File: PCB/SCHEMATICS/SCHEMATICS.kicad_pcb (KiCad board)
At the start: 2 copper layers, 95 parts, among them IC1 CP2102-GMR, Q1 PMOS, U1 C7433, U2 AMS1117-3.3, U3 LTR-303ALS-01, U4 AMS1117-3.3, U5 LTR-303ALS-01, U6 C6482, U7 C6482

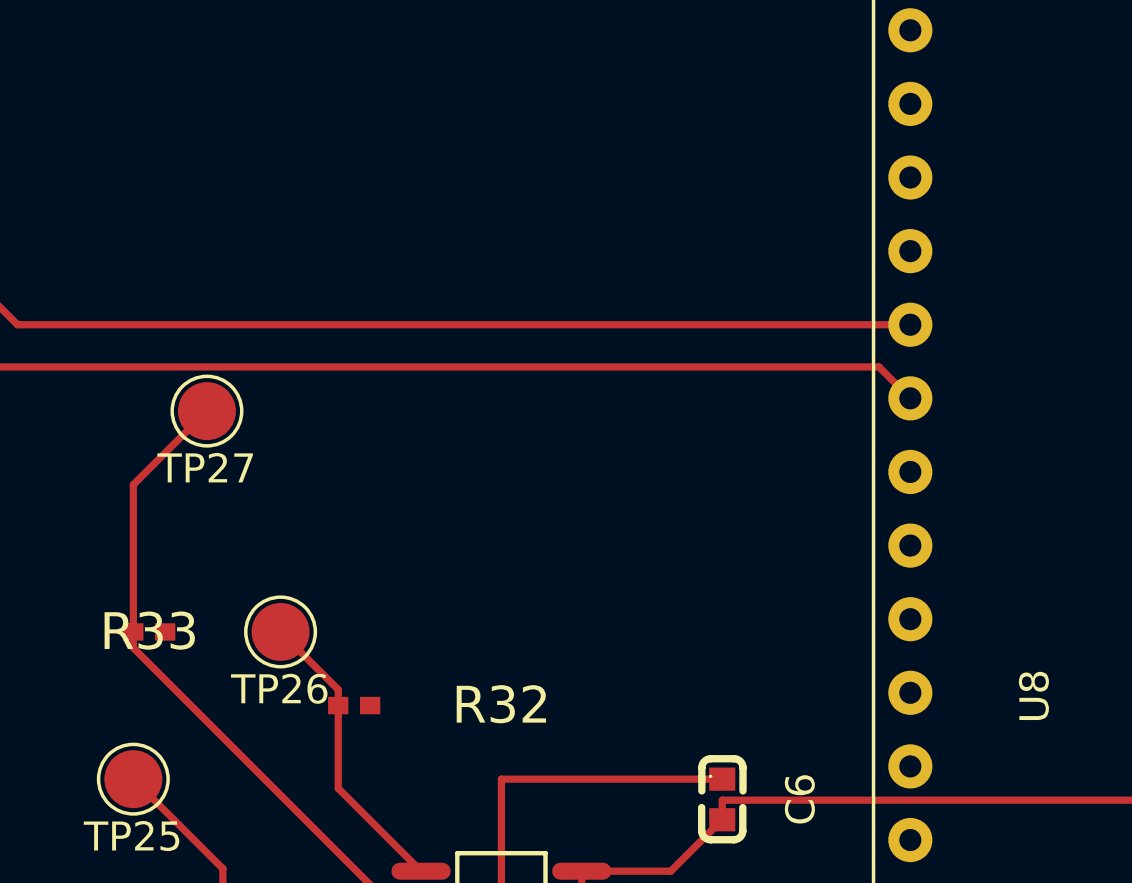
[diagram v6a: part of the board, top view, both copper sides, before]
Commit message: Creating ratsnest
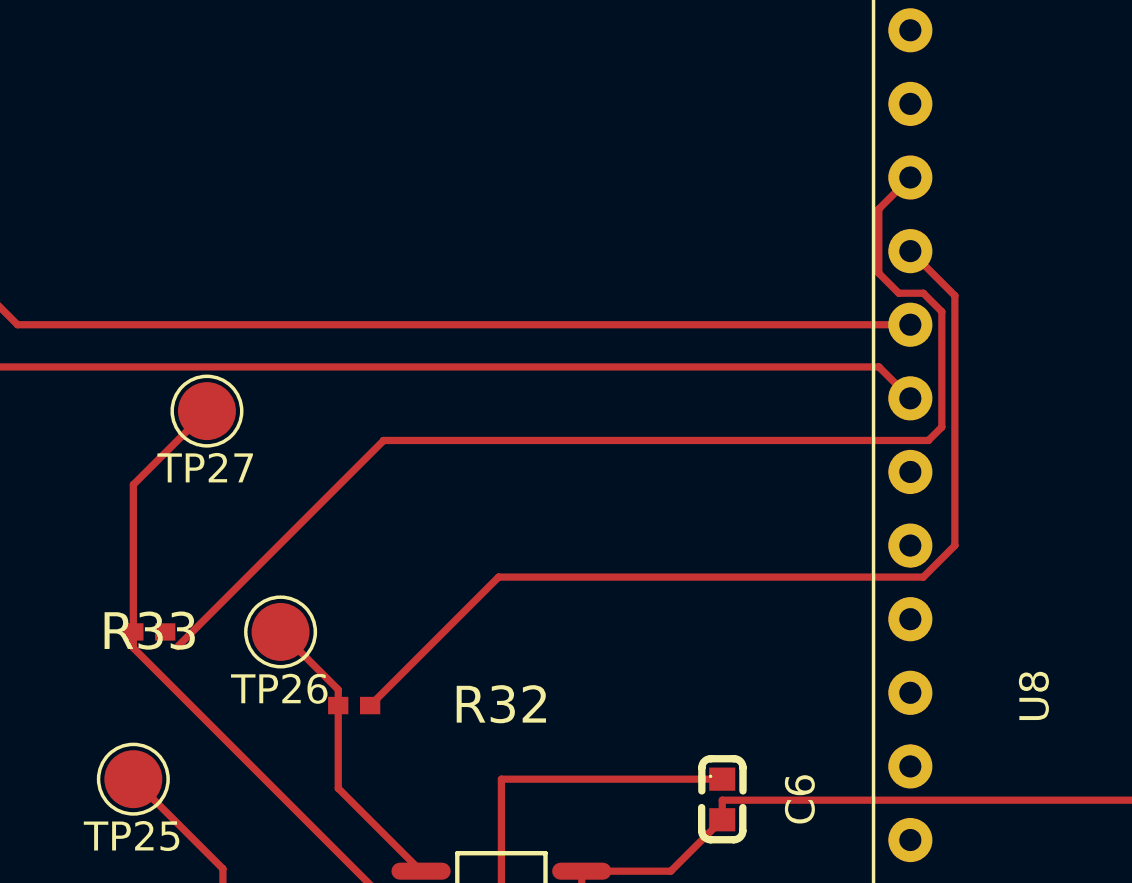
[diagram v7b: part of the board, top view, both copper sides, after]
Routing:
- net /MICROCONTROLLER/PA9: track 0.00 -> 40.0 mm
- net /MICROCONTROLLER/PA10: track 0.00 -> 33.3 mm
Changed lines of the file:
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@@
   (segment (start 162.36 77.3) (end 160.82 75.76) (width 0.25) (layer "F.Cu") (net 46))
   (segment (start 162.56 77.3) (end 162.36 77.3) (width 0.25) (layer "F.Cu") (net 46))
+  (segment (start 133.49 83.38) (end 132.403 84.467) (width 0.25) (layer "F.Cu") (net 52))
+  (segment (start 132.403 86.683) (end 133.093 87.373) (width 0.25) (layer "F.Cu") (net 52))
+  (segment (start 134.577 91.991) (end 134.115 92.453) (width 0.25) (layer "F.Cu") (net 52))
+  (segment (start 115.319 92.453) (end 108.204 99.568) (width 0.25) (layer "F.Cu") (net 52))
+  (segment (start 133.940251 87.373) (end 134.577 88.009749) (width 0.25) (layer "F.Cu") (net 52))
+  (segment (start 134.577 88.009749) (end 134.577 91.991) (width 0.25) (layer "F.Cu") (net 52))
+  (segment (start 133.093 87.373) (end 133.940251 87.373) (width 0.25) (layer "F.Cu") (net 52))
+  (segment (start 132.403 84.467) (end 132.403 86.683) (width 0.25) (layer "F.Cu") (net 52))
+  (segment (start 134.115 92.453) (end 115.319 92.453) (width 0.25) (layer "F.Cu") (net 52))
+  (segment (start 115.319 92.453) (end 115.316 92.456) (width 0.25) (layer "F.Cu") (net 52))
+  (segment (start 135.027 87.457) (end 135.027 96.080251) (width 0.25) (layer "F.Cu") (net 53))
+  (segment (start 135.027 96.080251) (end 133.940251 97.167) (width 0.25) (layer "F.Cu") (net 53))
+  (segment (start 133.49 85.92) (end 135.027 87.457) (width 0.25) (layer "F.Cu") (net 53))
+  (segment (start 133.940251 97.167) (end 119.283 97.167) (width 0.25) (layer "F.Cu") (net 53))
+  (segment (start 119.283 97.167) (end 114.85 101.6) (width 0.25) (layer "F.Cu") (net 53))
   (segment (start 102.684 88.46) (end 72.136 57.912) (width 0.25) (layer "F.Cu") (net 54))
   (segment (start 42.171619 60.452) (end 42.171619 60.163858) (width 0.25) (layer "F.Cu") (net 54))

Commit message: Added parallel headers and edge cuts
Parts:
- added J1: Conn_01x24_Pin, Connector_PinSocket_2.54mm:PinSocket_1x24_P2.54mm_Vertical, F.Cu at (173.6, 98.0)
- added J2: Conn_01x24_Pin, Connector_PinSocket_2.54mm:PinSocket_1x24_P2.54mm_Vertical, F.Cu at (115.3, 124.0)
- R40: value 510k -> Value: Value: Value: 510k
- moved C6 105.1 mm to (24.8, 80.2)
- moved R16 105.1 mm to (60.4, 52.1)
- moved R17 105.1 mm to (55.2, 38.9)
- moved R33 105.1 mm to (5.05, 74.5)
- moved TP13 105.1 mm to (68.0, 56.7)
- moved TP14 105.1 mm to (60.4, 38.9)
- moved TP15 105.1 mm to (60.4, 44.0)
- moved TP25 105.1 mm to (4.50, 79.5)
- moved TP26 105.1 mm to (9.58, 74.5)
- moved C4 105.1 mm to (70.5, 48.2)
- moved R18 105.1 mm to (65.5, 47.0)
- moved R19 105.1 mm to (54.9, 46.5)
- moved R32 105.1 mm to (12.1, 77.0)
- moved R34 105.1 mm to (7.04, 87.2)
- moved TP27 105.1 mm to (7.04, 66.8)
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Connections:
- U8 pad 14: unconnected-(U8-PA4-Pad14) -> /MICROCONTROLLER/PA4
- U8 pad 15: unconnected-(U8-PA5-Pad15) -> /MICROCONTROLLER/PA5
- U8 pad 16: unconnected-(U8-PA6-Pad16) -> /MICROCONTROLLER/PA6
- U8 pad 17: unconnected-(U8-PA7-Pad17) -> /MICROCONTROLLER/PA7
- U8 pad 18: unconnected-(U8-PB0-Pad18) -> /MICROCONTROLLER/PB0
- U8 pad 19: unconnected-(U8-PB1-Pad19) -> /MICROCONTROLLER/PB1
- U8 pad 2: unconnected-(U8-PC13-Pad2) -> /MICROCONTROLLER/PC13
- U8 pad 20: unconnected-(U8-PB2-Pad20) -> /MICROCONTROLLER/PB2
- U8 pad 25: unconnected-(U8-PB12-Pad25) -> /MICROCONTROLLER/PB12
- U8 pad 26: unconnected-(U8-PB13-Pad26) -> /MICROCONTROLLER/PB13
- U8 pad 27: unconnected-(U8-PB14-Pad27) -> /MICROCONTROLLER/PB14
- U8 pad 28: unconnected-(U8-PB15-Pad28) -> /MICROCONTROLLER/PB15
- U8 pad 29: unconnected-(U8-PA8-Pad29) -> /MICROCONTROLLER/PA8
- U8 pad 3: unconnected-(U8-PC14-Pad3) -> /MICROCONTROLLER/PC14
- U8 pad 34: unconnected-(U8-PA13-Pad34) -> /MICROCONTROLLER/PA13
- U8 pad 35: unconnected-(U8-PF6-Pad35) -> /MICROCONTROLLER/PF6
- U8 pad 36: unconnected-(U8-PF7-Pad36) -> /MICROCONTROLLER/PF7
- U8 pad 37: unconnected-(U8-PA14-Pad37) -> /MICROCONTROLLER/PA14
- U8 pad 38: unconnected-(U8-PA15-Pad38) -> /MICROCONTROLLER/PAQ15
- U8 pad 39: unconnected-(U8-PB3-Pad39) -> /MICROCONTROLLER/PB3
- U8 pad 4: unconnected-(U8-PC15-Pad4) -> /MICROCONTROLLER/PC15
- U8 pad 40: unconnected-(U8-PB4-Pad40) -> /MICROCONTROLLER/PB4
- U8 pad 41: unconnected-(U8-PB5-Pad41) -> /MICROCONTROLLER/PB5
- U8 pad 42: unconnected-(U8-PB6-Pad42) -> /MICROCONTROLLER/PB6
- U8 pad 43: unconnected-(U8-PB7-Pad43) -> /MICROCONTROLLER/PB7
- U8 pad 44: unconnected-(U8-BOOT-Pad44) -> /MICROCONTROLLER/BOOT
- U8 pad 45: unconnected-(U8-PB8-Pad45) -> /MICROCONTROLLER/PB8
- U8 pad 46: unconnected-(U8-PB9-Pad46) -> /MICROCONTROLLER/PB9
- U8 pad 5: unconnected-(U8-PF0-Pad5) -> /MICROCONTROLLER/PF0
- U8 pad 6: unconnected-(U8-PF1-Pad6) -> /MICROCONTROLLER/PF1
- U8 pad 7: unconnected-(U8-NRST-Pad7) -> /MICROCONTROLLER/NRST
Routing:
- net GND: track 464.4 -> 0.00 mm
- net /MICROCONTROLLER/VSS: track 329.9 -> 0.00 mm
- net /POWER MODULE/Battery: track 278.4 -> 0.00 mm
- net /MICROCONTROLLER/PA11: track 106.8 -> 0.00 mm
- net /MICROCONTROLLER/PA12: track 104.3 -> 0.00 mm
- net Net-(D5-K): track 59.1 -> 0.00 mm
- net /MICROCONTROLLER/PA9: track 40.0 -> 0.00 mm
- net /MICROCONTROLLER/PA10: track 33.3 -> 0.00 mm
- net Net-(U6-VCC): track 33.0 -> 0.00 mm
- net Net-(D2-K): track 32.8 -> 0.00 mm
- net /MICROCONTROLLER/PB10: track 24.9 -> 0.00 mm
- net Net-(TP4054-42-SOT25R1-BAT): track 23.1 -> 0.00 mm
- net Net-(U6-SCL): track 22.9 -> 0.00 mm
- net /MICROCONTROLLER/PA0: track 20.4 -> 0.00 mm
- net /MICROCONTROLLER/PA2: track 20.4 -> 0.00 mm
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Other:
- board outline added: 100 x 100 mm
